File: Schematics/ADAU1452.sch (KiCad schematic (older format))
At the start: 104 parts, among them CN201 COAX, P201 CONN_2x1, P202 CONN_2x1, P203 CONN_6X2, P204 CONN_6x1, SW201 SWITCH, SW202 SWITCH, U201 ADAU1452WBCPZ, U202 ADM13307-5ARZ, U203 25AA1024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

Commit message: Schematic and PCB changes
Changed and corrected some footprints, removed capacitors, updated
documentation to change 1v5 SMPS to 1v2. Have not removed 1v2 LDO from
schematic yet.
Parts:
- R207, R208, R209, R210, R211, R212, R213, R214, R215, R216: footprint OHDSP-Footprints-Pretty:SMD-0805 -> OHDSP-Footprints-Pretty:SMD-0603
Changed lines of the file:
@@
 F 0 "R208" V 5450 6550 40  0000 C CNN
 F 1 "0R" V 5407 6251 40  0000 C CNN
-F 2 "OHDSP-Footprints-Pretty:SMD-0805" V 5330 6250 30  0001 C CNN
+F 2 "OHDSP-Footprints-Pretty:SMD-0603" V 5330 6250 30  0001 C CNN
 F 3 "~" H 5400 6250 30  0000 C CNN
 	1    5400 6250
@@
 F 0 "R207" V 5450 6450 40  0000 C CNN
 F 1 "0R" V 5407 6151 40  0000 C CNN
-F 2 "OHDSP-Footprints-Pretty:SMD-0805" V 5330 6150 30  0001 C CNN
+F 2 "OHDSP-Footprints-Pretty:SMD-0603" V 5330 6150 30  0001 C CNN
 F 3 "~" H 5400 6150 30  0000 C CNN
 	1    5400 6150
@@
 F 0 "R209" V 5450 6650 40  0000 C CNN
 F 1 "0R" V 5407 6351 40  0000 C CNN
-F 2 "OHDSP-Footprints-Pretty:SMD-0805" V 5330 6350 30  0001 C CNN
+F 2 "OHDSP-Footprints-Pretty:SMD-0603" V 5330 6350 30  0001 C CNN
 F 3 "~" H 5400 6350 30  0000 C CNN
 	1    5400 6350
@@
 F 0 "R210" V 5450 6750 40  0000 C CNN
 F 1 "0R" V 5407 6451 40  0000 C CNN
-F 2 "OHDSP-Footprints-Pretty:SMD-0805" V 5330 6450 30  0001 C CNN
+F 2 "OHDSP-Footprints-Pretty:SMD-0603" V 5330 6450 30  0001 C CNN
 F 3 "~" H 5400 6450 30  0000 C CNN
 	1    5400 6450
@@
 F 0 "R213" V 5450 7050 40  0000 C CNN
 F 1 "0R" V 5407 6751 40  0000 C CNN
-F 2 "OHDSP-Footprints-Pretty:SMD-0805" V 5330 6750 30  0001 C CNN
+F 2 "OHDSP-Footprints-Pretty:SMD-0603" V 5330 6750 30  0001 C CNN
 F 3 "~" H 5400 6750 30  0000 C CNN
 	1    5400 6750
@@
 F 0 "R214" V 5450 7150 40  0000 C CNN
 F 1 "0R" V 5407 6851 40  0000 C CNN
-F 2 "OHDSP-Footprints-Pretty:SMD-0805" V 5330 6850 30  0001 C CNN
+F 2 "OHDSP-Footprints-Pretty:SMD-0603" V 5330 6850 30  0001 C CNN
 F 3 "~" H 5400 6850 30  0000 C CNN
 	1    5400 6850
@@
 F 0 "R212" V 5450 6950 40  0000 C CNN
 F 1 "N/F" V 5407 6651 40  0000 C CNN
-F 2 "OHDSP-Footprints-Pretty:SMD-0805" V 5330 6650 30  0001 C CNN
+F 2 "OHDSP-Footprints-Pretty:SMD-0603" V 5330 6650 30  0001 C CNN
 F 3 "~" H 5400 6650 30  0000 C CNN
 	1    5400 6650
@@
 F 0 "R211" V 5450 6850 40  0000 C CNN
 F 1 "N/F" V 5407 6551 40  0000 C CNN
-F 2 "OHDSP-Footprints-Pretty:SMD-0805" V 5330 6550 30  0001 C CNN
+F 2 "OHDSP-Footprints-Pretty:SMD-0603" V 5330 6550 30  0001 C CNN
 F 3 "~" H 5400 6550 30  0000 C CNN
 	1    5400 6550
@@
 F 0 "R215" V 5450 7250 40  0000 C CNN
 F 1 "N/F" V 5407 6951 40  0000 C CNN
-F 2 "OHDSP-Footprints-Pretty:SMD-0805" V 5330 6950 30  0001 C CNN
+F 2 "OHDSP-Footprints-Pretty:SMD-0603" V 5330 6950 30  0001 C CNN
 F 3 "~" H 5400 6950 30  0000 C CNN
 	1    5400 6950
@@
 F 0 "R216" V 5450 7350 40  0000 C CNN
 F 1 "N/F" V 5407 7051 40  0000 C CNN
-F 2 "OHDSP-Footprints-Pretty:SMD-0805" V 5330 7050 30  0001 C CNN
+F 2 "OHDSP-Footprints-Pretty:SMD-0603" V 5330 7050 30  0001 C CNN
 F 3 "~" H 5400 7050 30  0000 C CNN
 	1    5400 7050

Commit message: Change ADAU1452 footprint, minor PCB changes
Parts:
- U201: footprint OHDSP-Footprints-Pretty:IC-LFCSP72 -> OHDSP-Footprints-Pretty:IC-LFCSP72-HANDFIT
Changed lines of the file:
@@
 F 0 "U201" H 7600 1950 60  0000 C CNN
 F 1 "ADAU1452WBCPZ" H 7950 2050 60  0000 C CNN
-F 2 "OHDSP-Footprints-Pretty:IC-LFCSP72" H 6750 4100 60  0001 C CNN
+F 2 "OHDSP-Footprints-Pretty:IC-LFCSP72-HANDFIT" H 6750 4100 60  0001 C CNN
 F 3 "" H 6750 4100 60  0000 C CNN
 	1    6750 4100

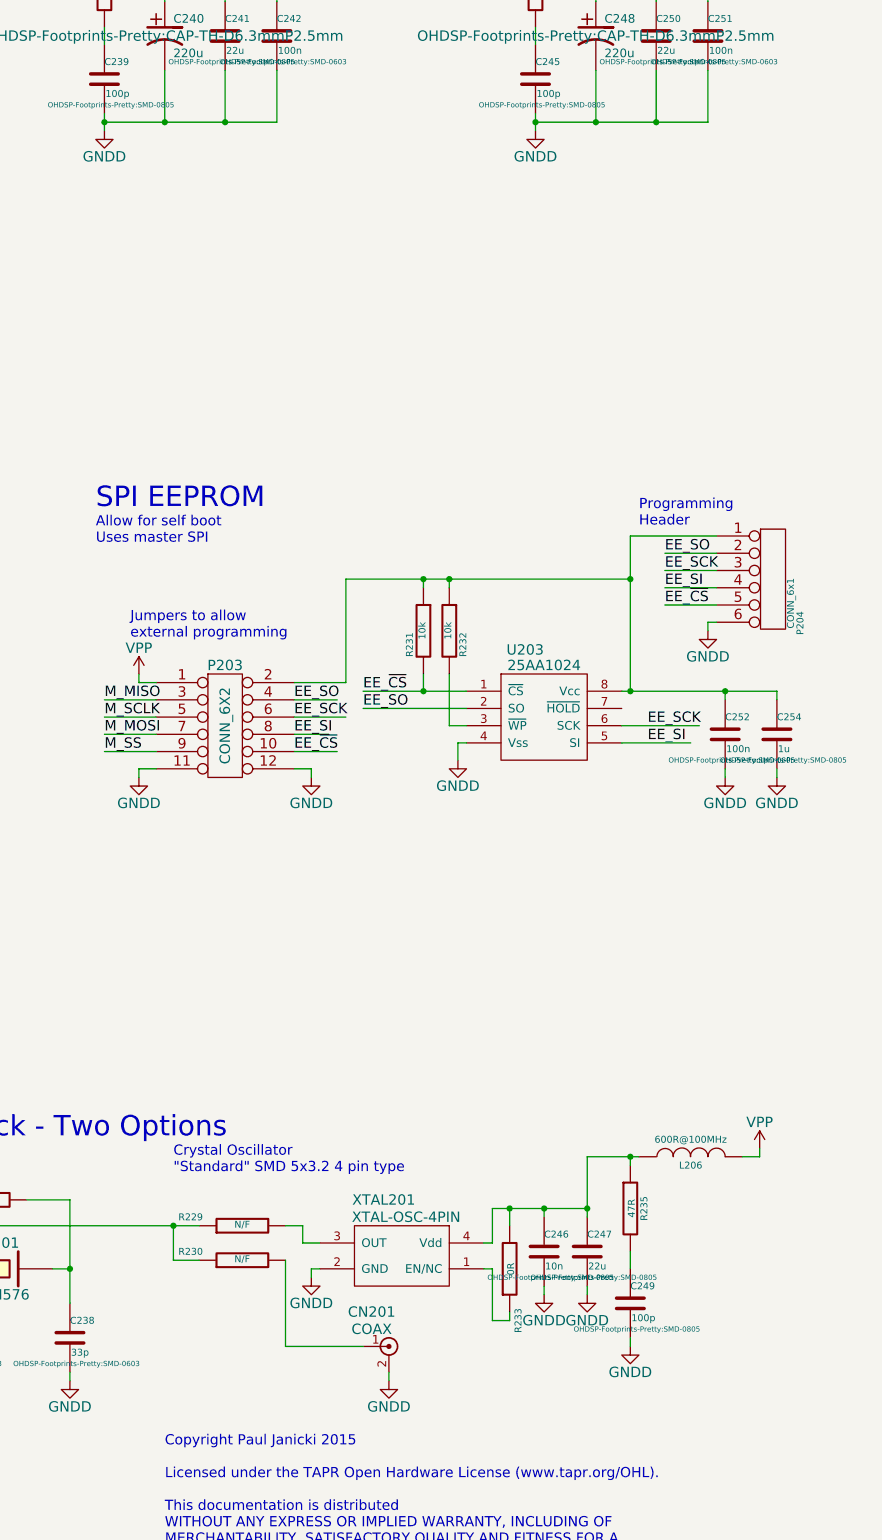
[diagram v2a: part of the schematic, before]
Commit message: Rationalise the clock and clock fan-out schematics.
Rationalise the clock and clock fan-out schematics.
Removed one clock fan out buffer, still have 4 master audio clock
outputs. Also removed local crytsal oscialltor, a low jitter crystal
should perform as well, ADAU1452 has internal "dejittering" anyway.
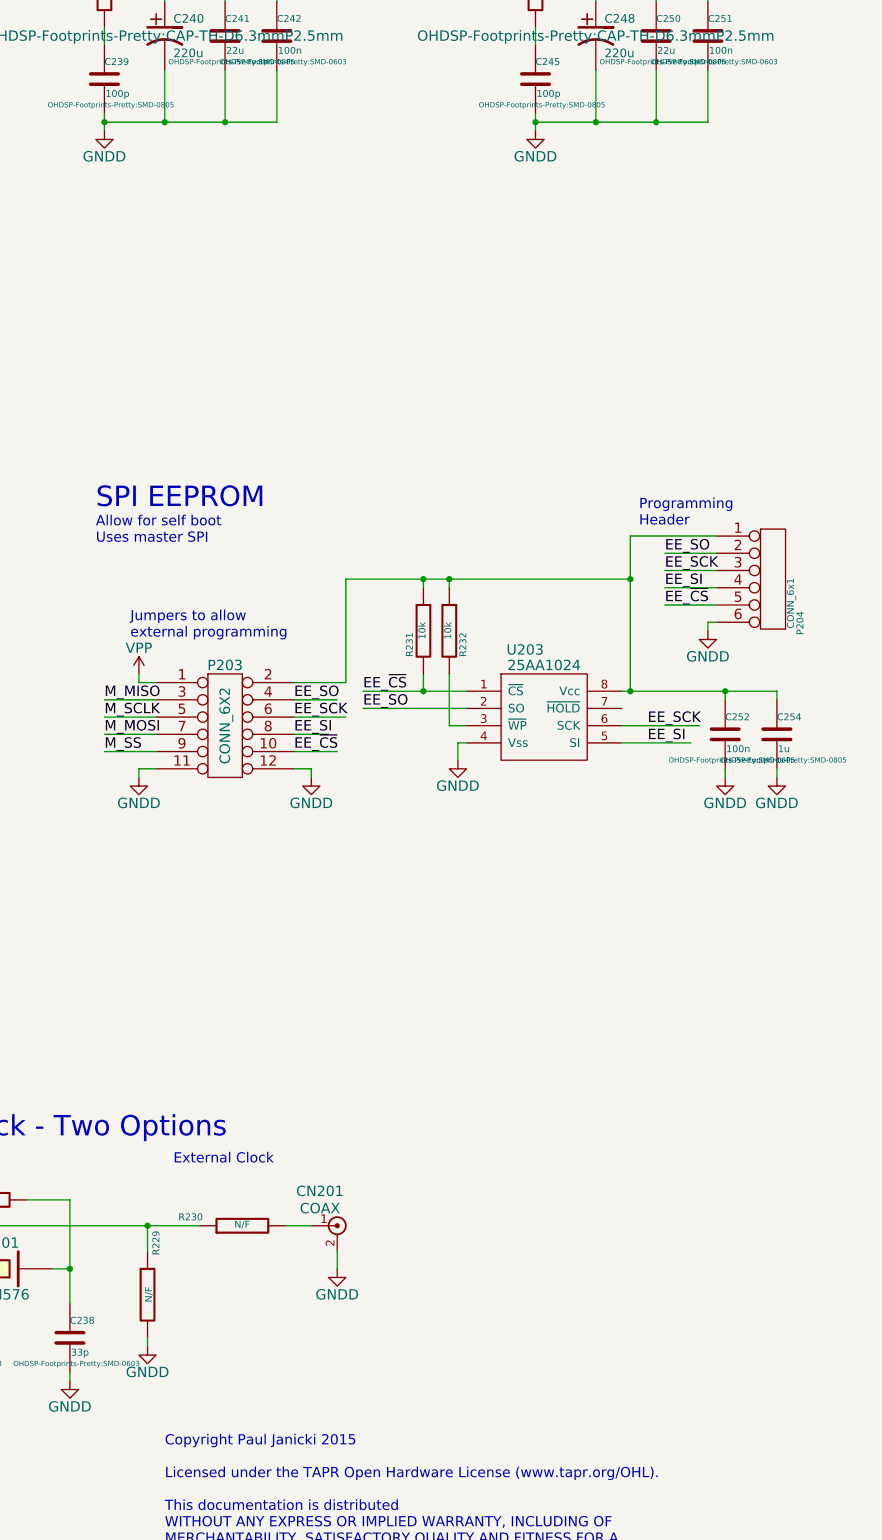
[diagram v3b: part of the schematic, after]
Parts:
- removed C246: 10n, OHDSP-Footprints-Pretty:SMD-0805, symbol C
- removed C247: 22u, OHDSP-Footprints-Pretty:SMD-0805, symbol C
- removed C249: 100p, OHDSP-Footprints-Pretty:SMD-0805, symbol C
- removed L206: 600R@100MHz, OHDSP-Footprints-Pretty:SMD-0805, symbol INDUCTOR
- removed R233: 0R, OHDSP-Footprints-Pretty:SMD-0805, symbol R
- removed R235: 47R, OHDSP-Footprints-Pretty:SMD-0805, symbol R
- removed XTAL201: XTAL-OSC-4PIN, OHDSP-Footprints-Pretty:XTAL_5x3.2_4PIN, symbol XTAL-OSC-4PIN
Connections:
- wire segments 344 -> 320
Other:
- note added: "External Clock"
- note removed: "Crystal Oscillator\n"Standard" SMD 5x3.2 4 pin type"
- moved on the sheet: CN201, R230
